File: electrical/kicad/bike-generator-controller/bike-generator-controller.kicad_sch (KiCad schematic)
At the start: 0 parts

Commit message: feat: add KiCad schematic hierarchy
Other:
- added sheet CC_CONTROL (cc_control.kicad_sch)
- added sheet CONNECTORS (connectors.kicad_sch)
- added sheet INA228_SENSE (ina228_sense.kicad_sch)
- added sheet MCU (mcu.kicad_sch)
- added sheet POWER_PATH (power_path.kicad_sch)
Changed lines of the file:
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@@
 	(generator_version "10.0")
 	(paper "A4")
+  (sheet
+    (at 25.4 38.1)
+    (size 63.5 38.1)
+    (exclude_from_sim no)
+    (in_bom yes)
+    (on_board yes)
+    (dnp no)
+    (fields_autoplaced yes)
+    (stroke (width 0.1524) (type solid))
+    (fill (color 0 0 0 0.0))
+    (property "Sheetname" "POWER_PATH"
+      (at 25.4 37.465 0)
+      (show_name no)
+      (do_not_autoplace no)
+      (effects (font (size 1.27 1.27)) (justify left bottom))
+    )
+    (property "Sheetfile" "power_path.kicad_sch"
+      (at 25.4 76.83500000000001 0)
+      (show_name no)
+      (do_not_autoplace no)
+      (effects (font (size 1.27 1.27)) (justify left top))
+    )
+    (instances
+      (project "bike-generator-controller"
+        (path "/3056615a-b94f-4555-a4c5-9bc697b25f9c" (page "2"))
+      )
+    )
+  )
+  (sheet
+    (at 101.6 38.1)
+    (size 63.5 38.1)
+    (exclude_from_sim no)
+    (in_bom yes)
+    (on_board yes)
+    (dnp no)
+    (fields_autoplaced yes)
+    (stroke (width 0.1524) (type solid))
+    (fill (color 0 0 0 0.0))
+    (property "Sheetname" "INA228_SENSE"
+      (at 101.6 37.465 0)
+      (show_name no)
+      (do_not_autoplace no)
+      (effects (font (size 1.27 1.27)) (justify left bottom))
+    )
+    (property "Sheetfile" "ina228_sense.kicad_sch"
+      (at 101.6 76.83500000000001 0)
+      (show_name no)
+      (do_not_autoplace no)
+      (effects (font (size 1.27 1.27)) (justify left top))
+    )
+    (instances
+      (project "bike-generator-controller"
+        (path "/3056615a-b94f-4555-a4c5-9bc697b25f9c" (page "3"))
+      )
+    )
+  )
+  (sheet
+    (at 177.8 38.1)
+    (size 63.5 38.1)
+    (exclude_from_sim no)
+    (in_bom yes)
+    (on_board yes)
+    (dnp no)
+    (fields_autoplaced yes)
+    (stroke (width 0.1524) (type solid))
+    (fill (color 0 0 0 0.0))
+    (property "Sheetname" "CONNECTORS"
+      (at 177.8 37.465 0)
+      (show_name no)
+      (do_not_autoplace no)
+      (effects (font (size 1.27 1.27)) (justify left bottom))
+    )
+    (property "Sheetfile" "connectors.kicad_sch"
+      (at 177.8 76.83500000000001 0)
+      (show_name no)
+      (do_not_autoplace no)
+      (effects (font (size 1.27 1.27)) (justify left top))
+    )
+    (instances
+      (project "bike-generator-controller"
+        (path "/3056615a-b94f-4555-a4c5-9bc697b25f9c" (page "4"))
+      )
+    )
+  )
+  (sheet
+    (at 101.6 101.6)
+    (size 63.5 38.1)
+    (exclude_from_sim no)
+    (in_bom yes)
+    (on_board yes)
+    (dnp no)
+    (fields_autoplaced yes)
+    (stroke (width 0.1524) (type solid))
+    (fill (color 0 0 0 0.0))
+    (property "Sheetname" "MCU"
+      (at 101.6 100.96499999999999 0)
+      (show_name no)
+      (do_not_autoplace no)
+      (effects (font (size 1.27 1.27)) (justify left bottom))
+    )
+    (property "Sheetfile" "mcu.kicad_sch"
+      (at 101.6 140.33499999999998 0)
+      (show_name no)
+      (do_not_autoplace no)
+      (effects (font (size 1.27 1.27)) (justify left top))
+    )
+    (instances
+      (project "bike-generator-controller"
+        (path "/3056615a-b94f-4555-a4c5-9bc697b25f9c" (page "5"))
+      )
+    )
+  )
+  (sheet
+    (at 177.8 101.6)
+    (size 63.5 38.1)
+    (exclude_from_sim no)
+    (in_bom yes)
+    (on_board yes)
+    (dnp no)
+    (fields_autoplaced yes)
+    (stroke (width 0.1524) (type solid))
+    (fill (color 0 0 0 0.0))
+    (property "Sheetname" "CC_CONTROL"
+      (at 177.8 100.96499999999999 0)
+      (show_name no)
+      (do_not_autoplace no)
+      (effects (font (size 1.27 1.27)) (justify left bottom))
+    )
+    (property "Sheetfile" "cc_control.kicad_sch"
+      (at 177.8 140.33499999999998 0)
+      (show_name no)
+      (do_not_autoplace no)
+      (effects (font (size 1.27 1.27)) (justify left top))
+    )
+    (instances
+      (project "bike-generator-controller"
+        (path "/3056615a-b94f-4555-a4c5-9bc697b25f9c" (page "6"))
+      )
+    )
+  )
+  (sheet_instances
+    (path "/"
+      (page "1")
+    )
+  )
+  (embedded_fonts no)
 )

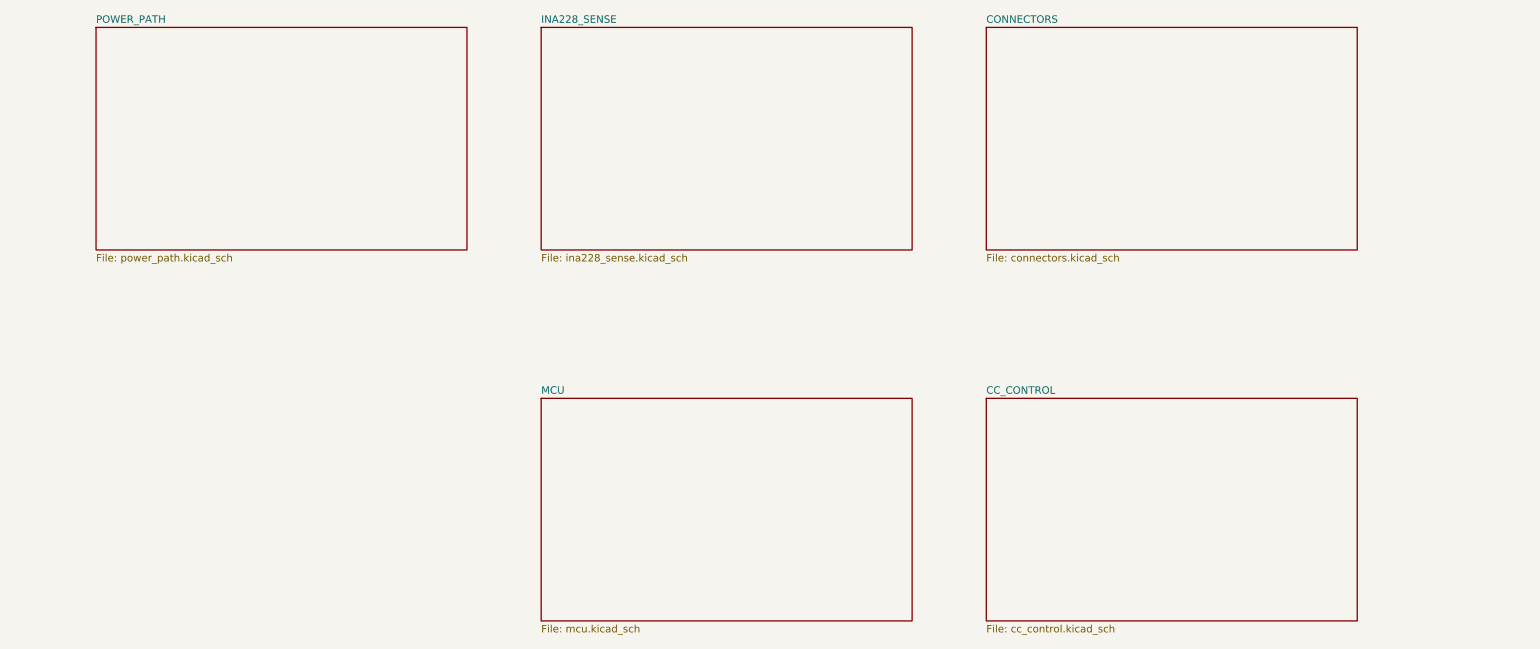
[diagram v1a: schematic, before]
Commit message: feat: integrate controller modules and schematics
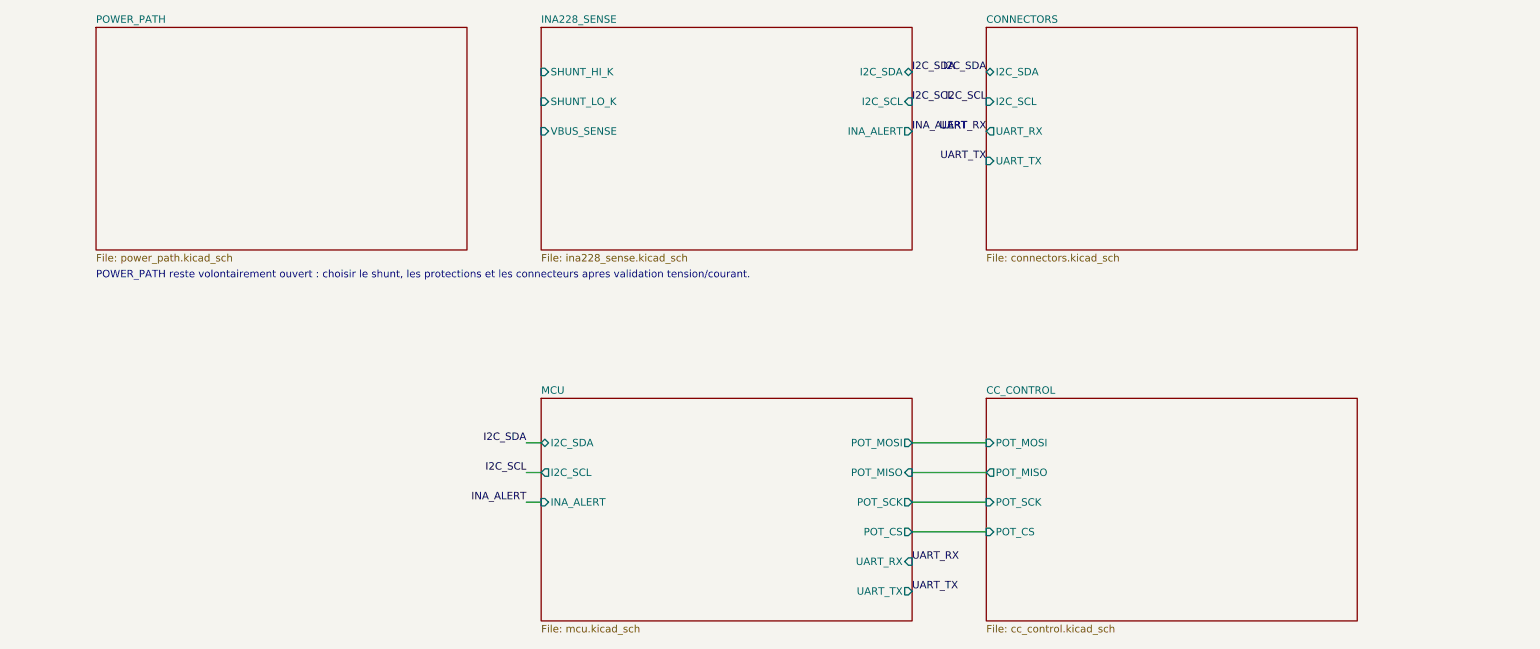
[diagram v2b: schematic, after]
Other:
- sheet CC_CONTROL ports: added POT_CS, POT_MISO, POT_MOSI, POT_SCK; removed none
- sheet CONNECTORS ports: added I2C_SCL, I2C_SDA, UART_RX, UART_TX; removed none
- sheet INA228_SENSE ports: added I2C_SCL, I2C_SDA, INA_ALERT, SHUNT_HI_K, SHUNT_LO_K, VBUS_SENSE; removed none
- sheet MCU ports: added I2C_SCL, I2C_SDA, INA_ALERT, POT_CS, POT_MISO, POT_MOSI, POT_SCK, UART_RX, UART_TX; removed none
- note added: "POWER_PATH reste volontairement ouvert : choisir le shunt, les protections et les connecteurs apres validation tension/courant."

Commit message: feat: build provisional power path schematic
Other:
- sheet POWER_PATH ports: added BUS_PROTECTED, SHUNT_HI_K, SHUNT_LO_K; removed none
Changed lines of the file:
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@@
+		)
+	)
+	(wire
+		(pts
+			(xy 88.9 45.72)
+			(xy 101.6 45.72)
+		)
+	)
+	(wire
+		(pts
+			(xy 88.9 50.8)
+			(xy 101.6 50.8)
+		)
+	)
+	(wire
+		(pts
+			(xy 88.9 55.88)
+			(xy 101.6 55.88)
 		)
 	)
@@
 			)
 		)
+		(pin "SHUNT_HI_K" output
+			(at 88.9 45.72 0)
+		)
+		(pin "SHUNT_LO_K" output
+			(at 88.9 50.8 0)
+		)
+		(pin "BUS_PROTECTED" output
+			(at 88.9 55.88 0)
+		)
 		(instances

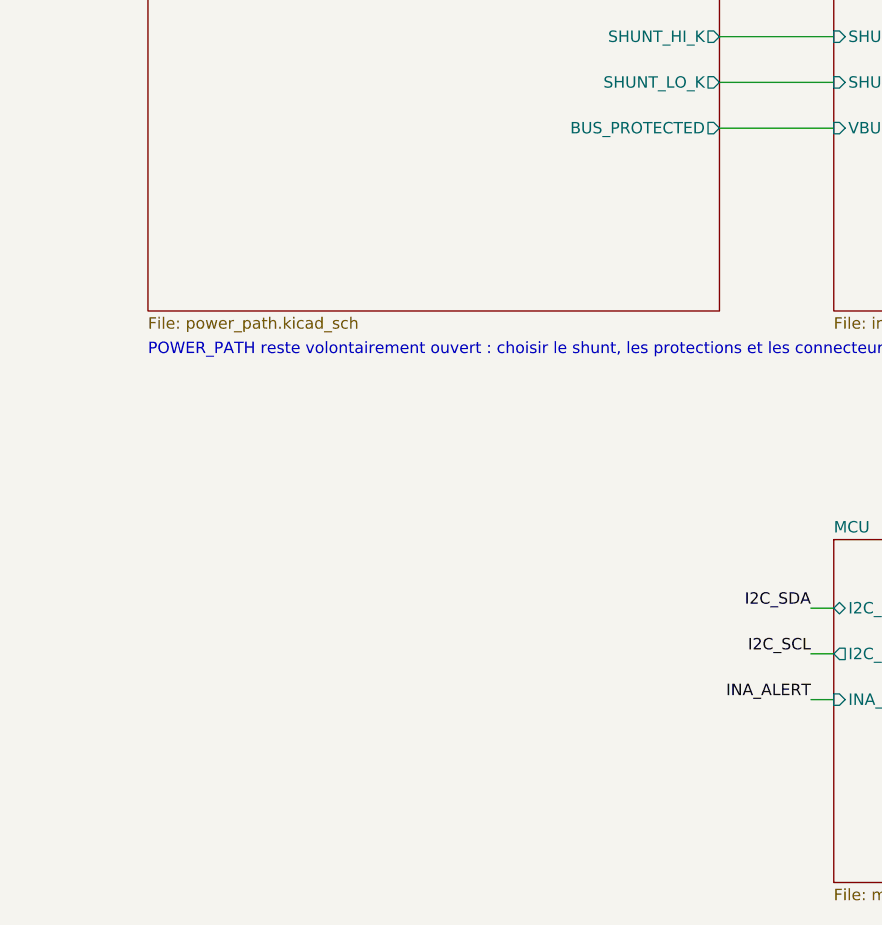
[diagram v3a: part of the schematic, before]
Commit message: feat: add LM5164 auxiliary supply schematic
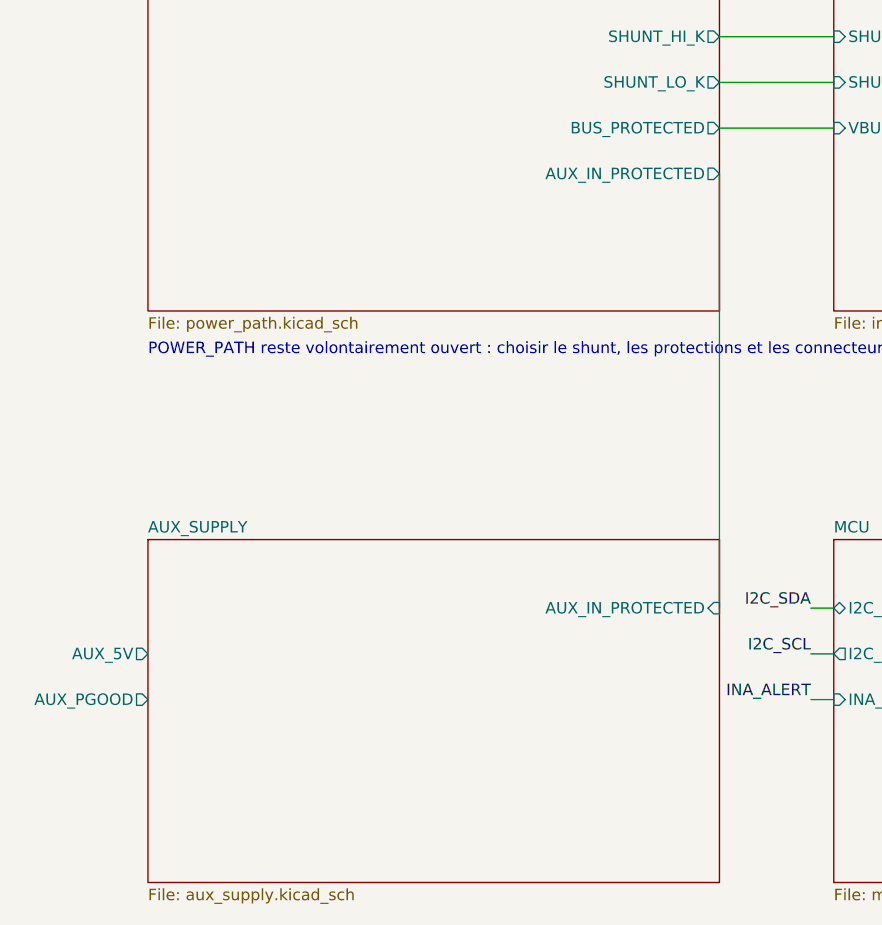
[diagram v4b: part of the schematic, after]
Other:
- added sheet AUX_SUPPLY (aux_supply.kicad_sch)
- sheet POWER_PATH ports: added AUX_IN_PROTECTED; removed none
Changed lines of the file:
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@@
+		)
+	)
+	(wire
+		(pts
+			(xy 88.9 60.96)
+			(xy 88.9 109.22)
 		)
 	)
@@
 			(at 88.9 55.88 0)
 		)
+		(pin "AUX_IN_PROTECTED" output
+			(at 88.9 60.96 0)
+		)
 		(instances
 			(project "bike-generator-controller"
@@
 				)
 			)
+		)
+	)
+	(sheet
+		(at 25.4 101.6)
+		(size 63.5 38.1)
+		(fields_autoplaced)
+		(exclude_from_sim no)
+		(in_bom yes)
+		(on_board yes)
+		(dnp no)
+		(stroke
+			(width 0.1524)
+			(type solid)
+		)
+		(fill
+			(color 0 0 0 0.0)
+		)
+		(property "Sheetname" "AUX_SUPPLY"
+			(at 25.4 100.96499999999999 0)
+			(show_name no)
+			(do_not_autoplace no)
+			(effects
+				(font
+					(size 1.27 1.27)
+				)
+				(justify left bottom)
+			)
+		)
+		(property "Sheetfile" "aux_supply.kicad_sch"
+			(at 25.4 140.33499999999998 0)
+			(show_name no)
+			(do_not_autoplace no)
+			(effects
+				(font
+					(size 1.27 1.27)
+				)
+				(justify left top)
+			)
+		)
+		(pin "AUX_IN_PROTECTED" input
+			(at 88.9 109.22 0)
+		)
+		(pin "AUX_5V" output
+			(at 25.4 114.3 0)
+		)
+		(pin "AUX_PGOOD" output
+			(at 25.4 119.38 0)
+		)
+		(instances
+			(project "bike-generator-controller"
+				(path "/3056615a-b94f-4555-a4c5-9bc697b25f9c"
+					(page "7")
+				)
+			)

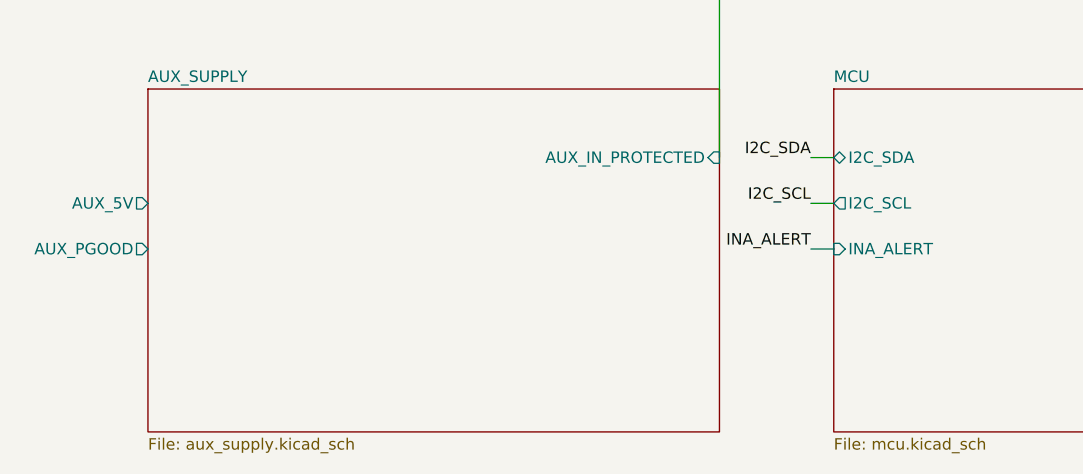
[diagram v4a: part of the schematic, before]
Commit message: feat: add MCU power interlock and battery input
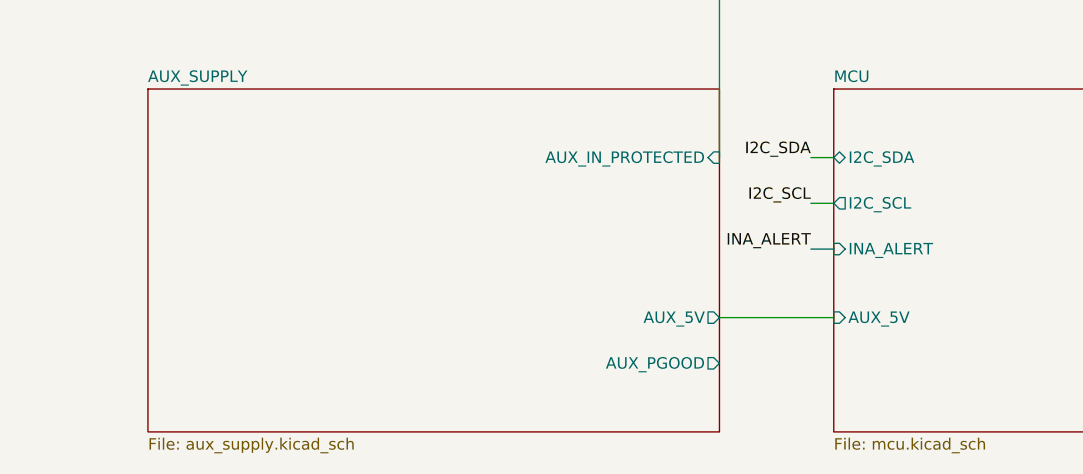
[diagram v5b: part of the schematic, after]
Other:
- sheet MCU ports: added AUX_5V; removed none
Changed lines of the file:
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@@
+		)
+	)
+	(wire
+		(pts
+			(xy 88.9 127)
+			(xy 101.6 127)
 		)
 	)
@@
 			(at 101.6 119.38 180)
 		)
+		(pin "AUX_5V" input
+			(at 101.6 127 180)
+		)
 		(instances
 			(project "bike-generator-controller"
@@
 		)
 		(pin "AUX_5V" output
-			(at 25.4 114.3 0)
+			(at 88.9 127 0)
 		)
 		(pin "AUX_PGOOD" output
-			(at 25.4 119.38 0)
-		)
-		(instances
+			(at 88.9 132.08 0)
+		)
+		(instances

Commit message: feat: establish controller PCB V1 design baseline
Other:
- sheet CC_CONTROL ports: added none; removed POT_MISO
- sheet MCU ports: added none; removed POT_MISO

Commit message: wip: checkpoint controller routing before review
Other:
- sheet CC_CONTROL ports: added POT_SHDN; removed none
- sheet CONNECTORS ports: added GPIO4_HALL, GPIO8_ACTION, POT_SHDN; removed UART_RX
- sheet MCU ports: added GPIO4_HALL, GPIO8_ACTION, POT_SHDN; removed UART_RX
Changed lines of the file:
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@@
+	(wire
+		(pts
+			(xy 176.53 129.54) (xy 207.01 129.54)
+		)
+		(stroke
+			(width 0)
+			(type default)
+		)
+	)
 	(wire
 		(pts
@@
 	(wire
 		(pts
+			(xy 195.58 73.66) (xy 195.58 137.16)
+		)
+		(stroke
+			(width 0)
+			(type default)
+		)
+	)
+	(wire
+		(pts
 			(xy 88.9 50.8) (xy 113.03 50.8)
 		)
@@
 	(wire
 		(pts
+			(xy 190.5 127) (xy 176.53 127)
+		)
+		(stroke
+			(width 0)
+			(type default)
+		)
+	)
+	(wire
+		(pts
 			(xy 88.9 60.96) (xy 92.71 60.96)
 		)
@@
 	(wire
 		(pts
+			(xy 190.5 68.58) (xy 190.5 127)
+		)
+		(stroke
+			(width 0)
+			(type default)
+		)
+	)
+	(wire
+		(pts
 			(xy 92.71 60.96) (xy 92.71 109.22)
 		)
@@
 	(wire
 		(pts
+			(xy 195.58 137.16) (xy 176.53 137.16)
+		)
+		(stroke
+			(width 0)
+			(type default)
+		)
+	)
+	(wire
+		(pts
+			(xy 207.01 73.66) (xy 195.58 73.66)
+		)
+		(stroke
+			(width 0)
+			(type default)
+		)
+	)
+	(wire
+		(pts
 			(xy 207.01 58.42) (xy 198.12 58.42)
 		)
@@
 		(pts
 			(xy 207.01 63.5) (xy 198.12 63.5)
+		)
+		(stroke
+			(width 0)
+			(type default)
+		)
+	)
+	(wire
+		(pts
+			(xy 207.01 68.58) (xy 190.5 68.58)
 		)
 		(stroke
@@
 		)
 	)
+	(label "POT_SHDN"
+		(at 176.53 129.54 0)
+		(effects
+			(font
+				(size 1.27 1.27)
+			)
+			(justify left bottom)
+		)
+	)
 	(label "UART_TX"
 		(at 176.53 134.62 0)
@@
 		)
 	)
-	(label "UART_RX"
-		(at 176.53 129.54 0)
-		(effects
-			(font
-				(size 1.27 1.27)
-			)
-			(justify left bottom)
-		)
-	)
 	(label "I2C_SCL"
 		(at 198.12 53.34 180)
@@
 		)
 	)
-	(label "UART_RX"
-		(at 198.12 58.42 180)
-		(effects
-			(font
-				(size 1.27 1.27)
-			)
-			(justify right bottom)
-		)
-	)
 	(label "INA_ALERT"
 		(at 110.49 119.38 180)
@@
 			)
 			(justify left bottom)
+		)
+	)
+	(label "POT_SHDN"
+		(at 198.12 58.42 180)
+		(effects
+			(font
+				(size 1.27 1.27)
+			)
+			(justify right bottom)
 		)
 	)
@@
 			)
 		)
-		(pin "UART_RX" output
+		(pin "POT_SHDN" input
 			(at 207.01 58.42 180)
+			(effects
+				(font
+					(size 1.27 1.27)
+				)
+				(justify left)
+			)
+		)
+		(pin "GPIO4_HALL" output
+			(at 207.01 68.58 180)
+			(effects
+				(font
+					(size 1.27 1.27)
+				)
+				(justify left)
+			)
+		)
+		(pin "GPIO8_ACTION" output
+			(at 207.01 73.66 180)
 			(effects
 				(font
@@
 		(at 113.03 101.6)
 		(size 63.5 38.1)
-		(fields_autoplaced)
 		(exclude_from_sim no)
 		(in_bom yes)
 		(on_board yes)
 		(dnp no)
+		(fields_autoplaced yes)
 		(stroke
 			(width 0.1524)
@@
 			)
 		)
-		(pin "UART_RX" input
+		(pin "POT_SHDN" output
 			(at 176.53 129.54 0)
 			(effects
@@
 				)
 				(justify left)
+			)
+		)
+		(pin "GPIO4_HALL" input
+			(at 176.53 127 0)
+			(effects
+				(font
+					(size 1.27 1.27)
+				)
+				(justify right)
+			)
+		)
+		(pin "GPIO8_ACTION" input
+			(at 176.53 137.16 0)
+			(effects
+				(font
+					(size 1.27 1.27)
+				)
+				(justify right)
 			)
 		)
@@
 		(at 207.01 101.6)
 		(size 63.5 38.1)
-		(fields_autoplaced)
 		(exclude_from_sim no)
 		(in_bom yes)
 		(on_board yes)
 		(dnp no)
+		(fields_autoplaced yes)
 		(stroke
 			(width 0.1524)
@@
 			(effects
 				(font
+					(size 1.27 1.27)
+				)
+				(justify left)
+			)
+		)
+		(pin "POT_SHDN" input
+			(at 207.01 129.54 180)
+			(effects
+				(font
